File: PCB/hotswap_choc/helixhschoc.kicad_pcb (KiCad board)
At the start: 2 copper layers, 135.2 x 94 mm, 134 parts, among them J1 MJ-4PP-9, P1 CONN_01X01, P2 CONN_01X01, P3 OLED, P4 LED, SW1 SW_PUSH, SW10 SW_PUSH, SW11 SW_PUSH, SW12 SW_PUSH, SW13 SW_PUSH, SW14 SW_PUSH, SW15 SW_PUSH, SW16 SW_PUSH, SW17 SW_PUSH, SW18 SW_PUSH, SW19 SW_PUSH, SW2 SW_PUSH, SW20 SW_PUSH, SW21 SW_PUSH, SW22 SW_PUSH, SW23 SW_PUSH, SW24 SW_PUSH, SW25 SW_PUSH, SW26 SW_PUSH, SW27 SW_PUSH, SW28 SW_PUSH, SW29 SW_PUSH, SW3 SW_PUSH, SW30 SW_PUSH, SW31 SW_PUSH, SW32 SW_PUSH, SW33 Reset, SW4 SW_PUSH, SW5 SW_PUSH, SW6 SW_PUSH, SW7 SW_PUSH, SW8 SW_PUSH, SW9 SW_PUSH, U1 ProMicro, U10 SK6812mini, U11 SK6812mini, U12 SK6812mini, U13 SK6812mini, U14 SK6812mini, U15 SK6812mini, U16 SK6812mini, U17 SK6812mini, U18 SK6812mini, U19 SK6812mini, U2 SK6812mini, U20 SK6812mini, U21 SK6812mini, U22 SK6812mini, U23 SK6812mini, U24 SK6812mini, U25 SK6812mini, U26 SK6812mini, U27 SK6812mini, U28 SK6812mini, U29 SK6812mini, U3 SK6812mini, U30 SK6812mini, U31 SK6812mini, U32 SK6812mini, U33 SK6812mini, U4 SK6812mini, U5 SK6812mini, U6 SK6812mini, U7 SK6812mini, U8 SK6812mini, U9 SK6812mini

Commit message: PCB WIP
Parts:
- J1: footprint MYLIB_REV:MJ-4PP-9_rev2 -> Random-keyboard-parts:MJ-4PP-9

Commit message: PCB WIP
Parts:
- removed the G*** at (196.5, 99.5) (x2)
- removed the G*** at (201.3, 92.4) (x2)
- removed the R1 at (208.0, 49.0) (x2)
- removed the R2 at (206.8, 52.8) (x2)
- added G***: Helix_logo_small, Logos:Helix_logo_small, B.Cu at (196.8, 95.6)
- added G***: LOGO, Logos:IronMan_small, B.Cu at (191.9, 102.7)
- added G***: Helix_logo_small, Logos:Helix_logo_small, F.Cu at (196.8, 95.6)
- added G***: LOGO, Logos:IronMan_small, F.Cu at (191.9, 102.7)
- added R1: 10k, Resistor_SMD:R_0805_2012Metric, F.Cu at (203.5, 52.2)
- added R1: 10k, Resistor_SMD:R_0805_2012Metric, B.Cu at (203.4, 52.2)
- added R2: 10k, Resistor_SMD:R_0805_2012Metric, B.Cu at (202.2, 56.0)
- added R2: 10k, Resistor_SMD:R_0805_2012Metric, F.Cu at (202.2, 56.0)
- SW33: footprint MYLIB:SW_3.5x6.0_TH -> Random-keyboard-parts:SW_3.5x6.0_TH
- U10, U11, U12, U13, U14, U15, U16, U17, U18, U19, U20, U21, U22, U23, U24, U25, U26, U27, U28, U29, U3, U30, U31, U32, U33, U4, U5, U6, U7, U8, U9: footprint MYLIB_REV:SK6812MINI_rev -> LED_WS_SK:SK6812MINI_rev
- U2: footprint JMG:SK6812MINI_rev -> LED_WS_SK:SK6812MINI_rev
- moved D24 15.1 mm to (174.2, 111.6), turned to 270 degrees
- moved D19 15.1 mm to (79.2, 111.6), turned to 270 degrees
- moved D20 15.1 mm to (98.2, 111.6), turned to 270 degrees
- moved D21 15.1 mm to (117.2, 111.6), turned to 270 degrees
- moved D22 15.1 mm to (136.2, 111.6), turned to 270 degrees
- moved D23 15.1 mm to (155.2, 111.6), turned to 270 degrees
- moved D25 15.0 mm to (193.2, 111.6), turned to 270 degrees
- moved J1 5.57 mm to (211.9, 90.4)
- moved G*** 5.57 mm to (142.2, 95.4)
- moved D11 5.57 mm to (163.2, 84.7)
- moved D18 5.57 mm to (182.3, 103.7)
- moved G*** 5.57 mm to (133.8, 92.4)
- moved H11 5.57 mm to (208.7, 83.7)
- moved JP11 5.57 mm to (198.5, 80.8)
- moved JP7 5.57 mm to (198.5, 80.8)
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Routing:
- net row4: track 246.2 -> 218.2 mm, vias 11 -> 17
- net row3: track 199.9 -> 188.3 mm, vias 10 -> 15
- net VCC: track 1047.3 -> 1057.6 mm, vias 41 -> 43
- net Net-(D19-Pad2): track 32.7 -> 23.5 mm
- net GND: track 919.6 -> 928.5 mm, vias 40 -> 37
- net Net-(D24-Pad2): track 31.1 -> 23.5 mm
- net Net-(D20-Pad2): track 31.0 -> 23.5 mm
- net Net-(D21-Pad2): track 31.0 -> 23.5 mm
- net Net-(D22-Pad2): track 31.0 -> 23.5 mm
- net Net-(D25-Pad2): track 31.0 -> 23.5 mm
- net Net-(D23-Pad2): track 31.0 -> 23.5 mm
- net col1: track 256.5 -> 263.9 mm, vias 7 -> 5
- net col2: track 225.7 -> 233.1 mm, vias 10 -> 8
- net col4: track 179.2 -> 186.5 mm, vias 8 -> 6
- net col0: track 296.4 -> 301.6 mm, vias 9 -> 7
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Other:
- outline, holes or cut-outs redrawn

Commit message: Pcb update
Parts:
- GND: renamed from JP11; footprint MYLIB:Jumper -> Random-keyboard-parts:Jumper_Small
- GND: renamed from JP4; footprint MYLIB:Jumper -> Random-keyboard-parts:Jumper_Small
- H10, H11, H12, H13: footprint JMG:HOLE_M2 -> Random-keyboard-parts:HOLE_M2
- P1, P2: footprint MYLIB:1PIN_0.1 -> Random-keyboard-parts:Pin_Small
- P3: footprint MYLIB:MY_SIL-4 -> Random-keyboard-parts:OLED_Small
- P4: footprint MYLIB_REV:StripLED_rev -> Random-keyboard-parts:LED_Strip_Pad
- SCL: renamed from JP9; footprint MYLIB:Jumper -> Random-keyboard-parts:Jumper_Small
- SCL: renamed from JP6; footprint MYLIB:Jumper -> Random-keyboard-parts:Jumper_Small
- SDA: renamed from JP8; footprint MYLIB:Jumper -> Random-keyboard-parts:Jumper_Small
- SDA: renamed from JP7; footprint MYLIB:Jumper -> Random-keyboard-parts:Jumper_Small
- VCC: renamed from JP10; footprint MYLIB:Jumper -> Random-keyboard-parts:Jumper_Small
- VCC: renamed from JP5; footprint MYLIB:Jumper -> Random-keyboard-parts:Jumper_Small
- moved P3 3.77 mm to (202.3, 84.0), turned to 0 degrees
- moved P4 2.53 mm to (189.9, 87.2)
- moved H13 1.42 mm to (195.9, 101.2)
- moved H10 1.42 mm to (209.6, 101.2)
- moved H12 1.42 mm to (195.9, 83.7)
- moved H11 0.91 mm to (209.6, 83.7)
- moved VCC 0.06 mm to (203.6, 80.9), turned to 0 degrees
- moved SDA 0.06 mm to (206.1, 80.9), turned to 180 degrees
- moved GND 0.06 mm to (206.1, 80.9), turned to 0 degrees
- moved SCL 0.06 mm to (201.1, 80.9), turned to 0 degrees
- moved SCL 0.06 mm to (203.6, 80.9), turned to 180 degrees
- moved VCC 0.06 mm to (201.0, 80.9), turned to 180 degrees
- turned GND to 180 degrees
- turned SDA to 0 degrees

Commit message: Update libs
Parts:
- D1, D10, D11, D12, D13, D14, D15, D16, D17, D18, D19, D2, D20, D21, D22, D23, D24, D25, D26, D27, D28, D29, D3, D30, D31, D32, D4, D5, D6, D7, D8, D9: footprint Random-keyboard-parts:D_SOD-123_dual_reversed -> cipulot_parts:D_SOD-123_dual_reversed
- GND (x2), SCL (x2), SDA (x2), VCC (x2): footprint Random-keyboard-parts:Jumper_Small -> cipulot_parts:Jumper_Small
- H1, H2, H3, H4, H5, H6, H7, H8, H9: footprint JMG:HOLE_M2_TH -> cipulot_parts:HOLE_M2_TH
- H10, H11, H12, H13: footprint Random-keyboard-parts:HOLE_M2 -> cipulot_parts:HOLE_M2
- J1: footprint Random-keyboard-parts:MJ-4PP-9 -> cipulot_parts:MJ-4PP-9
- P1, P2: footprint Random-keyboard-parts:Pin_Small -> cipulot_parts:Pin_Small
- P3: footprint Random-keyboard-parts:OLED_Small -> cipulot_parts:OLED_Small
- P4: footprint Random-keyboard-parts:LED_Strip_Pad -> cipulot_parts:LED_Strip_Pad
- SW33: footprint Random-keyboard-parts:SW_3.5x6.0_TH -> cipulot_parts:SW_3.5x6.0_TH
- U1: footprint Arduino:Sparkfun_Pro_Micro_reversible -> cipulot_parts:Sparkfun_Pro_Micro_reversible
- U10, U11, U12, U13, U14, U15, U16, U17, U18, U19, U2, U20, U21, U22, U23, U24, U25, U26, U27, U28, U29, U3, U30, U31, U32, U33, U4, U5, U6, U7, U8, U9: footprint LED_WS_SK:SK6812MINI_rev -> cipulot_parts:SK6812MINI_rev
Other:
- board text removed: "P3"

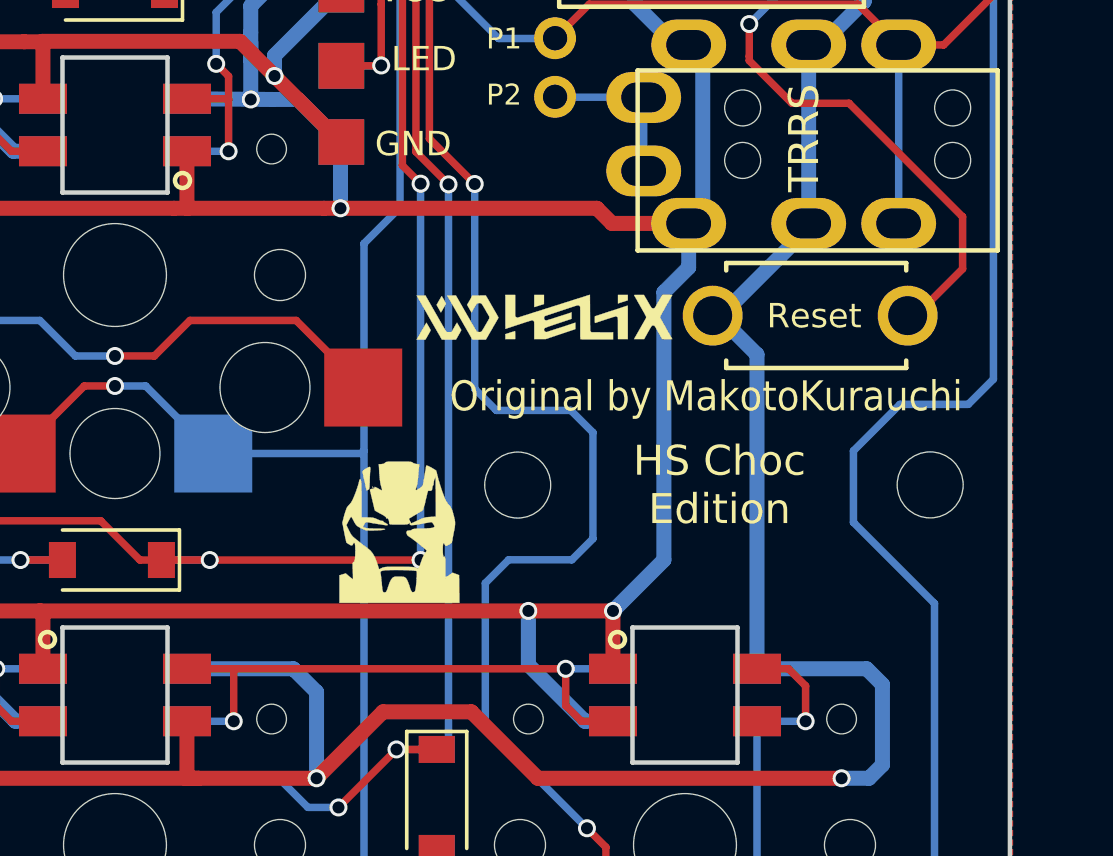
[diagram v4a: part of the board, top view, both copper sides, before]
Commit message: Update 3d model and some wiring
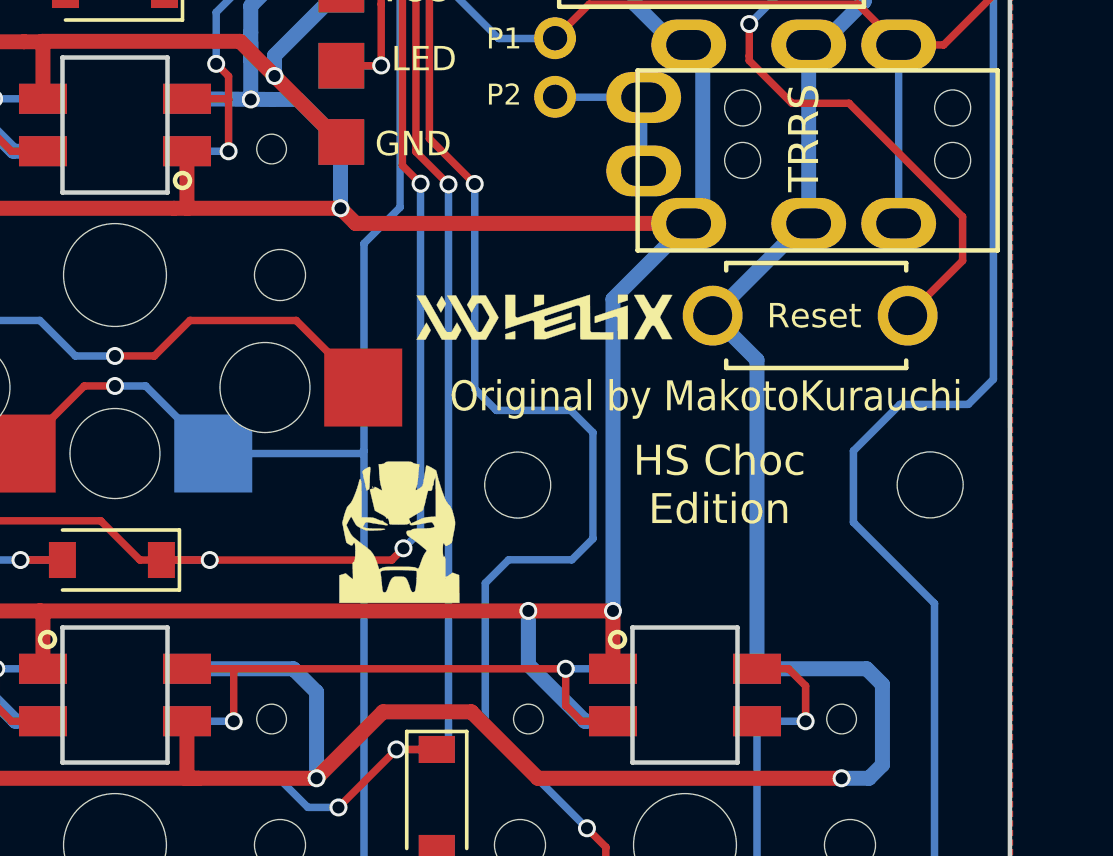
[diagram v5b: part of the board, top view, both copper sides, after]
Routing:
- net row2: track 173.9 -> 173.2 mm

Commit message: Update PCB
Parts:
- SW1, SW10, SW11, SW12, SW13, SW14, SW15, SW16, SW17, SW18, SW19, SW2, SW20, SW21, SW22, SW23, SW24, SW25, SW26, SW27, SW28, SW29, SW3, SW30, SW31, SW32, SW4, SW5, SW6, SW7, SW8, SW9: footprint Keyswitches:Kailh_socket_PG1350_reversible_LEFT_nosilkangle -> cipulot_parts:Kailh_socket_PG1350_reversible_LEFT_nosilkangle
- renumbered VCC to JP10, GND to JP11, GND to JP4, VCC to JP5, SCL to JP6, SDA to JP7, SDA to JP8, SCL to JP9
